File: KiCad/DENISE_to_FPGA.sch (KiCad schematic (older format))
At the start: 16 parts, among them J1 Conn_01x02, J2 Conn_01x02, J3 Conn_01x40, U1 LM1117-3.3, U2 74LVC162244A, U3 74LVC1G57GV, U4 Denise_MB_PinHeader

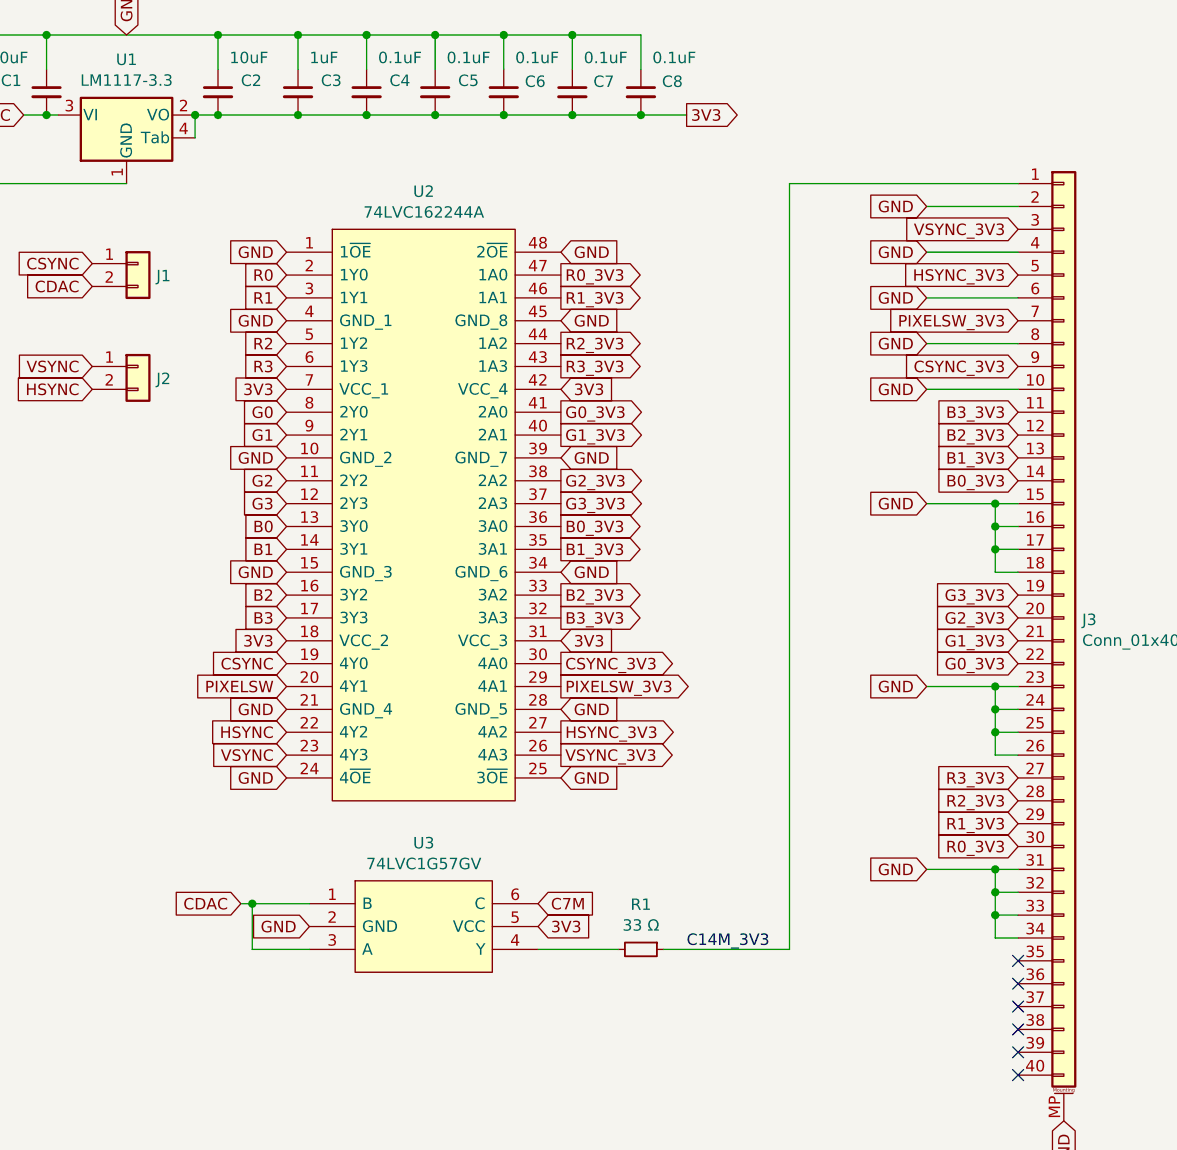
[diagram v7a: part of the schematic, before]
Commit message: Fixed orientation of U2
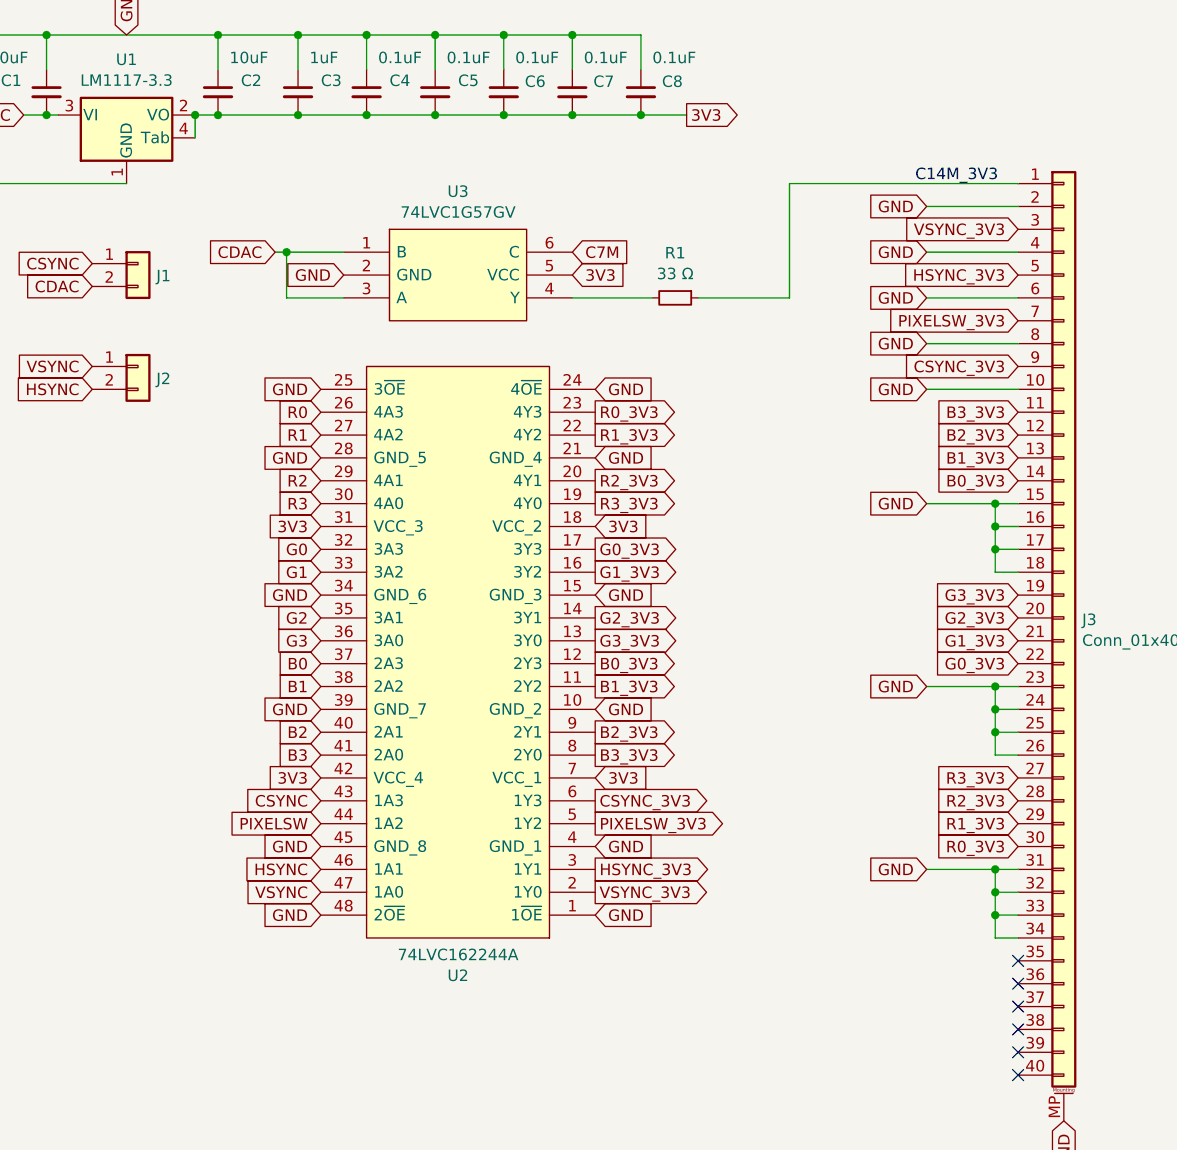
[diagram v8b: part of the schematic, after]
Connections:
- net B0: now also U2.37 (2A3); no longer U2.13 (3Y0)
- net B0_3V3: now also U2.12 (2Y3); no longer U2.36 (3A0)
- net B1: now also U2.38 (2A2); no longer U2.14 (3Y1)
- net B1_3V3: now also U2.11 (2Y2); no longer U2.35 (3A1)
- net B2: now also U2.40 (2A1); no longer U2.16 (3Y2)
- net B2_3V3: now also U2.9 (2Y1); no longer U2.33 (3A2)
- net B3: now also U2.41 (2A0); no longer U2.17 (3Y3)
- net B3_3V3: now also U2.8 (2Y0); no longer U2.32 (3A3)
- net CSYNC: now also U2.43 (1A3); no longer U2.19 (4Y0)
- net CSYNC_3V3: now also U2.6 (1Y3); no longer U2.30 (4A0)
- net G0: now also U2.32 (3A3); no longer U2.8 (2Y0)
- net G0_3V3: now also U2.17 (3Y3); no longer U2.41 (2A0)
- net G1: now also U2.33 (3A2); no longer U2.9 (2Y1)
- net G1_3V3: now also U2.16 (3Y2); no longer U2.40 (2A1)
- net G2: now also U2.35 (3A1); no longer U2.11 (2Y2)
- net G2_3V3: now also U2.14 (3Y1); no longer U2.38 (2A2)
- net G3: now also U2.36 (3A0); no longer U2.12 (2Y3)
- net G3_3V3: now also U2.13 (3Y0); no longer U2.37 (2A3)
- net HSYNC: now also U2.46 (1A1); no longer U2.22 (4Y2)
- net HSYNC_3V3: now also U2.3 (1Y1); no longer U2.27 (4A2)
- net PIXELSW: now also U2.44 (1A2); no longer U2.20 (4Y1)
- net PIXELSW_3V3: now also U2.5 (1Y2); no longer U2.29 (4A1)
- net R0: now also U2.26 (4A3); no longer U2.2 (1Y0)
- net R0_3V3: now also U2.23 (4Y3); no longer U2.47 (1A0)
- net R1: now also U2.27 (4A2); no longer U2.3 (1Y1)
- net R1_3V3: now also U2.22 (4Y2); no longer U2.46 (1A1)
- net R2: now also U2.29 (4A1); no longer U2.5 (1Y2)
- net R2_3V3: now also U2.20 (4Y1); no longer U2.44 (1A2)
- net R3: now also U2.30 (4A0); no longer U2.6 (1Y3)
- net R3_3V3: now also U2.19 (4Y0); no longer U2.43 (1A3)
- net VSYNC: now also U2.47 (1A0); no longer U2.23 (4Y3)
- net VSYNC_3V3: now also U2.2 (1Y0); no longer U2.26 (4A3)
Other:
- moved on the sheet: R1, U2, U3
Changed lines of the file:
@@
 Text GLabel 4800 3000 2    50   Input ~ 0
 GND
-Text GLabel 7250 2000 0    50   Input ~ 0
+Text GLabel 7400 2600 0    50   Input ~ 0
 R1
-Text GLabel 7250 1900 0    50   Input ~ 0
+Text GLabel 7400 2500 0    50   Input ~ 0
 R0
-Text GLabel 7250 2300 0    50   Input ~ 0
+Text GLabel 7400 2900 0    50   Input ~ 0
 R3
-Text GLabel 7250 2200 0    50   Input ~ 0
+Text GLabel 7400 2800 0    50   Input ~ 0
 R2
-Text GLabel 7250 3000 0    50   Input ~ 0
+Text GLabel 7400 3600 0    50   Input ~ 0
 B0
-Text GLabel 7250 2600 0    50   Input ~ 0
+Text GLabel 7400 3200 0    50   Input ~ 0
 G1
-Text GLabel 7250 2500 0    50   Input ~ 0
+Text GLabel 7400 3100 0    50   Input ~ 0
 G0
-Text GLabel 7250 3300 0    50   Input ~ 0
+Text GLabel 7400 3900 0    50   Input ~ 0
 B2
-Text GLabel 7250 3400 0    50   Input ~ 0
+Text GLabel 7400 4000 0    50   Input ~ 0
 B3
-Text GLabel 7250 3100 0    50   Input ~ 0
+Text GLabel 7400 3700 0    50   Input ~ 0
 B1
-Text GLabel 7250 2900 0    50   Input ~ 0
+Text GLabel 7400 3500 0    50   Input ~ 0
 G3
-Text GLabel 7250 2800 0    50   Input ~ 0
+Text GLabel 7400 3400 0    50   Input ~ 0
 G2
-Text GLabel 8450 3000 2    50   Output ~ 0
+Text GLabel 8600 3600 2    50   Output ~ 0
 B0_3V3
-Text GLabel 8450 3300 2    50   Output ~ 0
+Text GLabel 8600 3900 2    50   Output ~ 0
 B2_3V3
-Text GLabel 8450 3100 2    50   Output ~ 0
+Text GLabel 8600 3700 2    50   Output ~ 0
 B1_3V3
-Text GLabel 8450 3400 2    50   Output ~ 0
+Text GLabel 8600 4000 2    50   Output ~ 0
 B3_3V3
-Text GLabel 8450 1900 2    50   Output ~ 0
+Text GLabel 8600 2500 2    50   Output ~ 0
 R0_3V3
-Text GLabel 8450 2900 2    50   Output ~ 0
+Text GLabel 8600 3500 2    50   Output ~ 0
 G3_3V3
-Text GLabel 8450 2000 2    50   Output ~ 0
+Text GLabel 8600 2600 2    50   Output ~ 0
 R1_3V3
-Text GLabel 8450 2800 2    50   Output ~ 0
+Text GLabel 8600 3400 2    50   Output ~ 0
 G2_3V3
-Text GLabel 8450 2600 2    50   Output ~ 0
+Text GLabel 8600 3200 2    50   Output ~ 0
 G1_3V3
-Text GLabel 8450 2500 2    50   Output ~ 0
+Text GLabel 8600 3100 2    50   Output ~ 0
 G0_3V3
-Text GLabel 8450 2200 2    50   Output ~ 0
+Text GLabel 8600 2800 2    50   Output ~ 0
 R2_3V3
-Text GLabel 8450 2300 2    50   Output ~ 0
+Text GLabel 8600 2900 2    50   Output ~ 0
 R3_3V3
 $Comp
@@
 	7900 850  7600 850
 Connection ~ 7600 850
-Text GLabel 7250 3500 0    50   Input ~ 0
+Text GLabel 7400 4100 0    50   Input ~ 0
 3V3
-Text GLabel 8450 2400 2    50   Input ~ 0
+Text GLabel 8600 3000 2    50   Input ~ 0
 3V3
-Text GLabel 7250 2100 0    50   Input ~ 0
-GND
-Text GLabel 7250 2700 0    50   Input ~ 0
+Text GLabel 7400 2700 0    50   Input ~ 0
+GND
+Text GLabel 7400 3300 0    50   Input ~ 0
 GND
 $Comp
@@
 Text GLabel 10450 2500 0    50   Input ~ 0
 B3_3V3
-Text GLabel 7250 2400 0    50   Input ~ 0
+Text GLabel 7400 3000 0    50   Input ~ 0
 3V3
-Text GLabel 7250 3200 0    50   Input ~ 0
-GND
-Text GLabel 7250 3800 0    50   Input ~ 0
-GND
-Text GLabel 7250 3700 0    50   Input ~ 0
+Text GLabel 7400 3800 0    50   Input ~ 0
+GND
+Text GLabel 7400 4400 0    50   Input ~ 0
+GND
+Text GLabel 7400 4300 0    50   Input ~ 0
 PIXELSW
-Text GLabel 8450 3700 2    50   Output ~ 0
+Text GLabel 8600 4300 2    50   Output ~ 0
 PIXELSW_3V3
 Text GLabel 10450 3300 0    50   Input ~ 0
@@
 Text GLabel 10450 3600 0    50   Input ~ 0
 G0_3V3
-Text GLabel 8450 3500 2    50   Input ~ 0
+Text GLabel 8600 4100 2    50   Input ~ 0
 3V3
 Wire Wire Line
@@
 Text GLabel 10650 5600 3    50   Input ~ 0
 GND
-Text GLabel 7250 3900 0    50   Input ~ 0
+Text GLabel 7400 4500 0    50   Input ~ 0
 HSYNC
-Text GLabel 8450 3900 2    50   Output ~ 0
+Text GLabel 8600 4500 2    50   Output ~ 0
 HSYNC_3V3
 Text GLabel 10450 1900 0    50   Input ~ 0
 HSYNC_3V3
-Text GLabel 7250 4000 0    50   Input ~ 0
+Text GLabel 7400 4600 0    50   Input ~ 0
 VSYNC
-Text GLabel 8450 4000 2    50   Output ~ 0
+Text GLabel 8600 4600 2    50   Output ~ 0
 VSYNC_3V3
 Text GLabel 10450 1700 0    50   Input ~ 0
@@
 L Device:R_Small R1
 U 1 1 64FE39F6
-P 8800 4850
-F 0 "R1" V 8604 4850 50  0000 C CNN
-F 1 "33 Ω" V 8695 4850 50  0000 C CNN
-F 2 "Resistor_SMD:R_0805_2012Metric_Pad1.20x1.40mm_HandSolder" H 8800 4850 50  0001 C CNN
-F 3 "~" H 8800 4850 50  0001 C CNN
-	1    8800 4850
+P 8950 2000
+F 0 "R1" V 8754 2000 50  0000 C CNN
+F 1 "33 Ω" V 8845 2000 50  0000 C CNN
+F 2 "Resistor_SMD:R_0805_2012Metric_Pad1.20x1.40mm_HandSolder" H 8950 2000 50  0001 C CNN
+F 3 "~" H 8950 2000 50  0001 C CNN
+	1    8950 2000
 	0    1    1    0
 $EndComp
-Text Label 9000 4850 0    50   ~ 0
+Text Label 10000 1500 0    50   ~ 0
 C14M_3V3
 NoConn ~ 10450 5400
@@
 L DENISE_to_FPGA:74LVC162244A U2
 U 1 1 66EA62DE
-P 7850 2900
-F 0 "U2" H 7850 4265 50  0000 C CNN
-F 1 "74LVC162244A" H 7850 4174 50  0000 C CNN
-F 2 "Package_SO:TSSOP-48_6.1x12.5mm_P0.5mm" H 8300 4100 50  0001 L CNN
-F 3 "" H 8300 4000 50  0001 L CNN
-	1    7850 2900
-	1    0    0    -1
-$EndComp
-Text GLabel 7250 1800 0    50   Input ~ 0
-GND
-Text GLabel 7250 4100 0    50   Input ~ 0
-GND
-Text GLabel 8450 4100 2    50   Input ~ 0
-GND
-Text GLabel 8450 3800 2    50   Input ~ 0
-GND
-Text GLabel 8450 3200 2    50   Input ~ 0
-GND
-Text GLabel 8450 2700 2    50   Input ~ 0
-GND
-Text GLabel 8450 2100 2    50   Input ~ 0
-GND
-Text GLabel 8450 1800 2    50   Input ~ 0
+P 8000 3600
+F 0 "U2" H 8000 4965 50  0000 C CNN
+F 1 "74LVC162244A" H 8000 4874 50  0000 C CNN
+F 2 "Package_SO:TSSOP-48_6.1x12.5mm_P0.5mm" H 8450 4800 50  0001 L CNN
+F 3 "" H 8450 4700 50  0001 L CNN
+	1    8000 3600
+	-1   0    0    1
+$EndComp
+Text GLabel 7400 2400 0    50   Input ~ 0
+GND
+Text GLabel 7400 4700 0    50   Input ~ 0
+GND
+Text GLabel 8600 4700 2    50   Input ~ 0
+GND
+Text GLabel 8600 4400 2    50   Input ~ 0
+GND
+Text GLabel 8600 3800 2    50   Input ~ 0
+GND
+Text GLabel 8600 3300 2    50   Input ~ 0
+GND
+Text GLabel 8600 2700 2    50   Input ~ 0
+GND
+Text GLabel 8600 2400 2    50   Input ~ 0
 GND
 Text GLabel 6400 1950 0    50   Input ~ 0
@@
 Text GLabel 4800 3550 2    50   Input ~ 0
 CSYNC
-Text GLabel 7250 3600 0    50   Input ~ 0
+Text GLabel 7400 4200 0    50   Input ~ 0
 CSYNC
-Text GLabel 8450 3600 2    50   Output ~ 0
+Text GLabel 8600 4200 2    50   Output ~ 0
 CSYNC_3V3
 Text GLabel 6400 1850 0    50   Input ~ 0
@@
 	9000 1200 8800 1200
 Connection ~ 8800 1200
-Text GLabel 8350 4750 2    50   Input ~ 0
+Text GLabel 8500 1900 2    50   Input ~ 0
 3V3
-Text GLabel 7050 4650 0    50   Input ~ 0
+Text GLabel 7200 1800 0    50   Input ~ 0
 CDAC
-Text GLabel 7350 4750 0    50   Input ~ 0
+Text GLabel 7500 1900 0    50   Input ~ 0
 GND
 Wire Wire Line
 	9450 1500 10450 1500
-Text GLabel 8350 4650 2    50   Input ~ 0
+Text GLabel 8500 1800 2    50   Input ~ 0
 C7M
 $Comp
 L DENISE_to_FPGA:74LVC1G57GV U3
 U 1 1 66FF807E
-P 7850 4750
-F 0 "U3" H 7850 5115 50  0000 C CNN
-F 1 "74LVC1G57GV" H 7850 5024 50  0000 C CNN
-F 2 "Package_SO:TSOP-6_1.65x3.05mm_P0.95mm" H 8200 4950 50  0001 L CNN
-F 3 "" H 8200 4850 50  0001 L CNN
-	1    7850 4750
-	1    0    0    -1
-$EndComp
-Wire Wire Line
-	9450 1500 9450 4850
-Wire Wire Line
-	8900 4850 9450 4850
-Wire Wire Line
-	8350 4850 8700 4850
-Wire Wire Line
-	7050 4650 7100 4650
-Wire Wire Line
-	7100 4650 7100 4850
-Wire Wire Line
-	7100 4850 7350 4850
-Connection ~ 7100 4650
-Wire Wire Line
-	7100 4650 7350 4650
+P 8000 1900
+F 0 "U3" H 8000 2265 50  0000 C CNN
+F 1 "74LVC1G57GV" H 8000 2174 50  0000 C CNN
+F 2 "Package_SO:TSOP-6_1.65x3.05mm_P0.95mm" H 8350 2100 50  0001 L CNN
+F 3 "" H 8350 2000 50  0001 L CNN
+	1    8000 1900
+	1    0    0    -1
+$EndComp
+Wire Wire Line
+	8500 2000 8850 2000
+Wire Wire Line
+	7200 1800 7250 1800
+Wire Wire Line
+	7250 1800 7250 2000
+Wire Wire Line
+	7250 2000 7500 2000
+Connection ~ 7250 1800
+Wire Wire Line
+	7250 1800 7500 1800
+Wire Wire Line
+	9450 2000 9450 1500
+Wire Wire Line
+	9050 2000 9450 2000
 $EndSCHEMATC
